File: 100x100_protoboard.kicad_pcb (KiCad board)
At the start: 2 copper layers, 97.8 x 96.5 mm, 418 parts, among them CON1 BARREL_JACK, CON2 USB_FEMALE_WITH_ID, CON3 USB_FEMALE_WITH_ID, J1 INTERCONNECT_1X03, J10 INTERCONNECT_1X03, J11 INTERCONNECT_1X03, J12 INTERCONNECT_1X03, J13 INTERCONNECT_1X03, J14 INTERCONNECT_1X03, J15 INTERCONNECT_1X03, J16 INTERCONNECT_1X03, J17 INTERCONNECT_1X03, J18 INTERCONNECT_1X03, J19 INTERCONNECT_1X03, J2 INTERCONNECT_1X03, J20 INTERCONNECT_1X03, J21 INTERCONNECT_1X03, J22 INTERCONNECT_1X03, J23 INTERCONNECT_1X03, J24 INTERCONNECT_1X03, J25 INTERCONNECT_1X03, J26 INTERCONNECT_1X03, J27 INTERCONNECT_1X03, J28 INTERCONNECT_1X03, J29 INTERCONNECT_1X03, J3 INTERCONNECT_1X03, J30 INTERCONNECT_1X03, J31 INTERCONNECT_1X03, J32 INTERCONNECT_1X03, J33 INTERCONNECT_1X03, J34 INTERCONNECT_1X03, J35 INTERCONNECT_1X03, J36 INTERCONNECT_1X03, J37 INTERCONNECT_1X03, J38 INTERCONNECT_1X03, J39 INTERCONNECT_1X03, J4 INTERCONNECT_1X03, J40 INTERCONNECT_1X03, J41 INTERCONNECT_1X03, J42 INTERCONNECT_1X03, J43 INTERCONNECT_1X03, J44 INTERCONNECT_1X03, J45 INTERCONNECT_1X03, J46 INTERCONNECT_1X03, J47 INTERCONNECT_1X03, J48 INTERCONNECT_1X03, J49 INTERCONNECT_1X03, J5 INTERCONNECT_1X03, J50 INTERCONNECT_1X03, J51 INTERCONNECT_1X03, J52 INTERCONNECT_1X03, J53 INTERCONNECT_1X03, J54 INTERCONNECT_1X03, J55 INTERCONNECT_1X03, J56 INTERCONNECT_1X03, J57 INTERCONNECT_1X03, J58 INTERCONNECT_1X03, J59 INTERCONNECT_1X03, J6 INTERCONNECT_1X03, J60 INTERCONNECT_1X03, J61 INTERCONNECT_1X03, J62 INTERCONNECT_1X03, J63 INTERCONNECT_1X03, J64 INTERCONNECT_1X03, J65 INTERCONNECT_1X02, J7 INTERCONNECT_1X03, J8 INTERCONNECT_1X03, J9 INTERCONNECT_1X03, P1 CONN_5, P1 CONN_8X2, P2 CONN_8X2, U1 LM7805CT

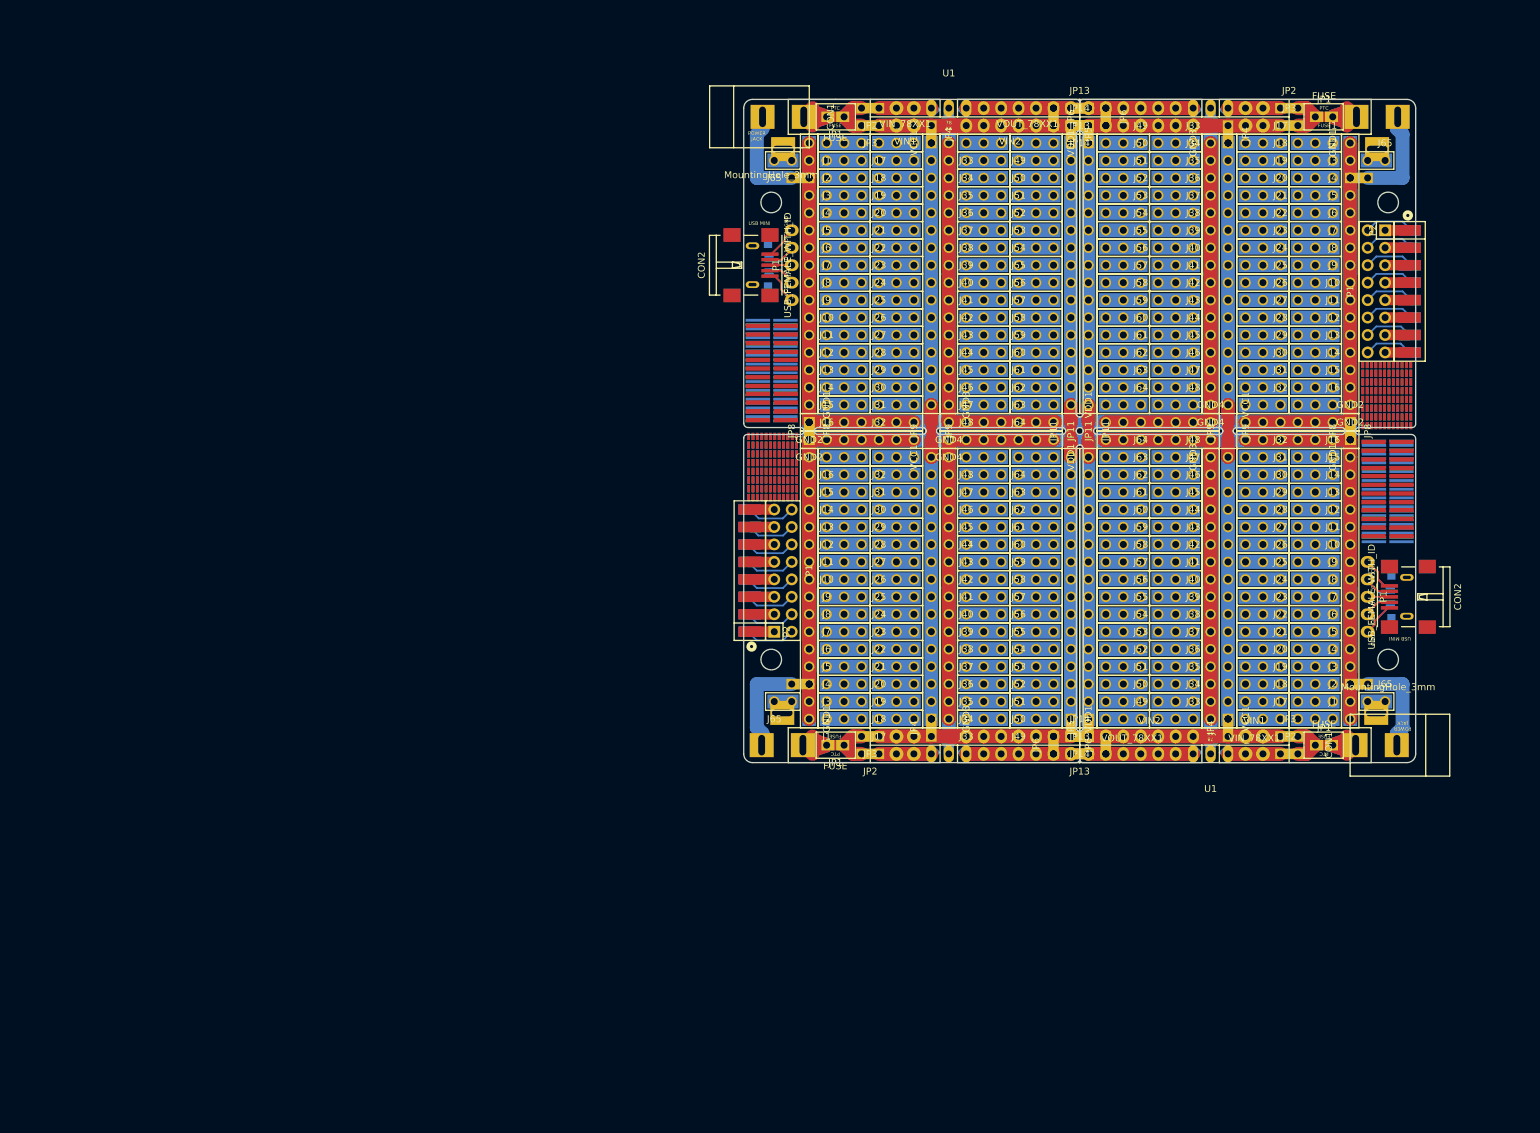
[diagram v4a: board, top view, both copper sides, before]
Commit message: flipped the outermost power rail solder jumper, so that all of these solder-jumpers are shorted on the front
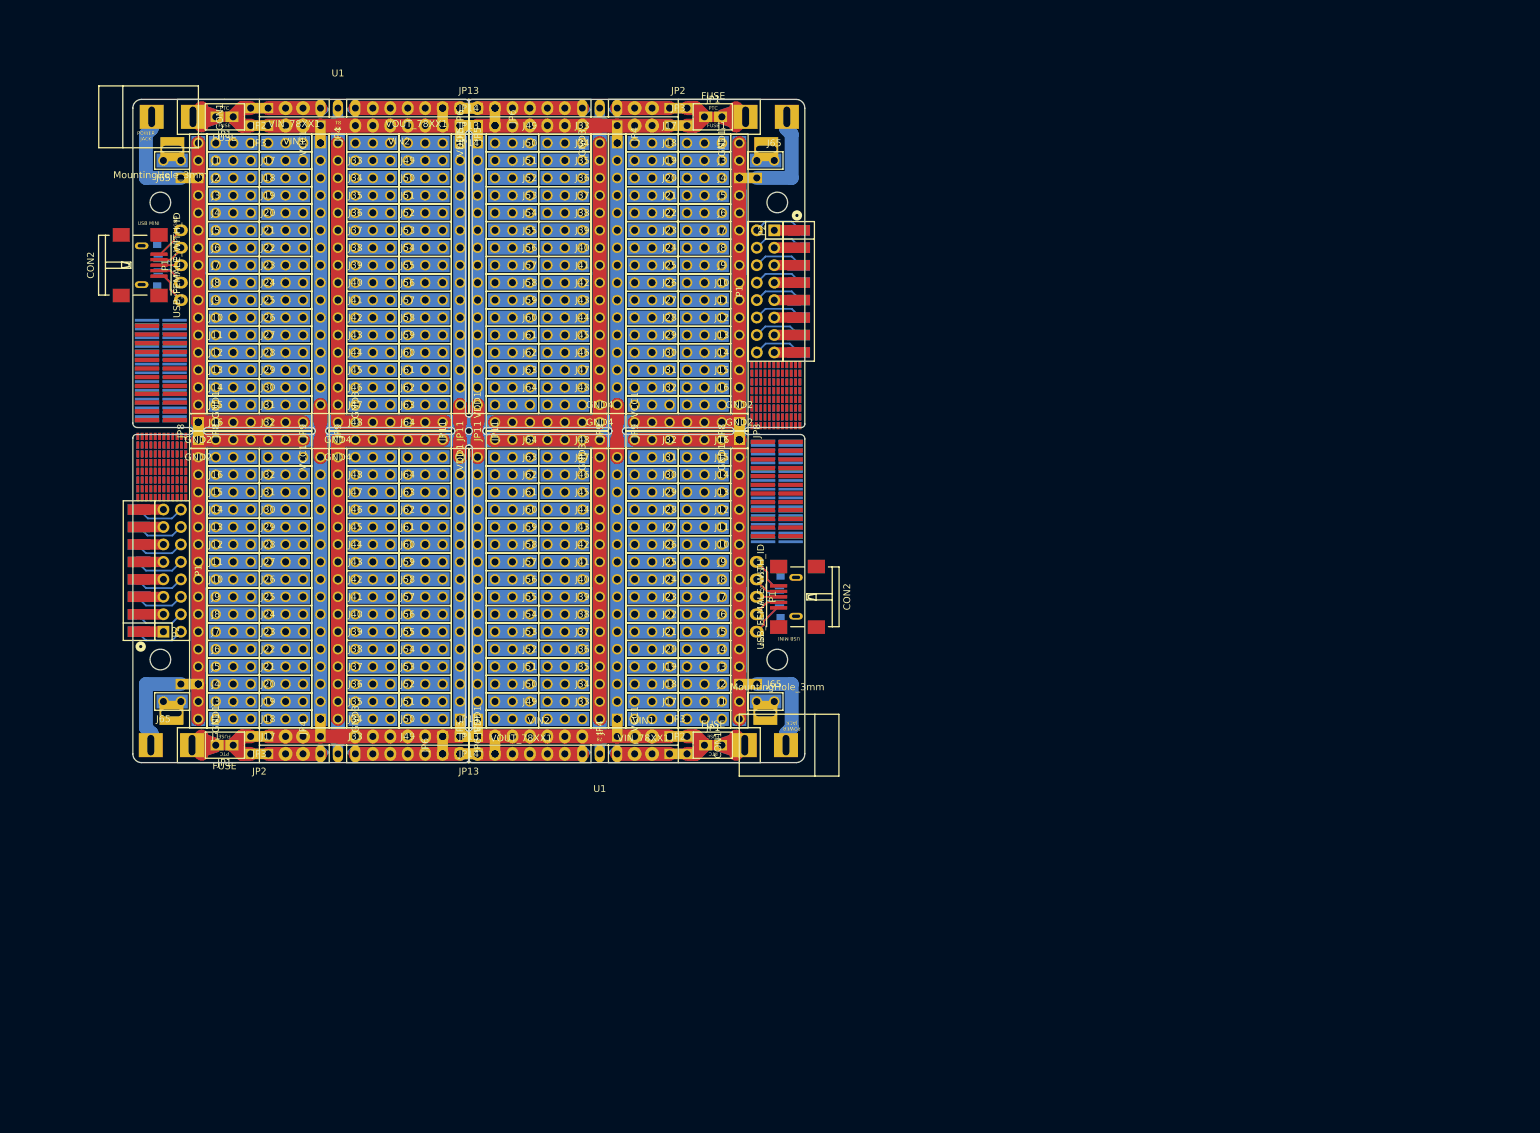
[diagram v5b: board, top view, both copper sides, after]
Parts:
- removed the C1 at (190.5, 32.8)
- removed the C1 at (190.5, 124.7)
- removed the C2 at (188.0, 32.8)
- removed the C2 at (188.0, 124.7)
- removed the CON1 at (216.7, 33.0)
- removed the CON1 at (216.5, 124.5)
- removed the F1 at (205.7, 33.0)
- removed the F1 at (205.7, 124.5)
- removed the F2 at (205.7, 33.0)
- removed the F2 at (205.7, 124.5)
- removed the GND1 at (209.6, 36.8)
- removed the GND1 at (209.6, 82.5)
- removed the GND2 at (209.6, 77.5)
- removed the GND2 at (209.6, 80.0)
- removed the GND3 at (189.2, 36.8)
- removed the GND3 at (189.2, 82.5)
- removed the GND4 at (189.2, 77.5)
- removed the GND4 at (189.2, 80.0)
- removed the J1 at (207.0, 36.8)
- removed the J1 at (207.0, 120.7)
- removed the J10 at (207.0, 59.7)
- removed the J10 at (207.0, 97.8)
- removed the J11 at (207.0, 62.2)
- removed the J11 at (207.0, 95.2)
- removed the J12 at (207.0, 64.8)
- removed the J12 at (207.0, 92.7)
- removed the J13 at (207.0, 67.3)
- removed the J13 at (207.0, 90.2)
- removed the J14 at (207.0, 69.8)
- removed the J14 at (207.0, 87.6)
- removed the J15 at (207.0, 72.4)
- removed the J15 at (207.0, 85.1)
- removed the J16 at (207.0, 74.9)
- removed the J16 at (207.0, 82.5)
- removed the J17 at (199.4, 36.8)
- removed the J17 at (199.4, 120.7)
- removed the J18 at (199.4, 39.4)
- removed the J18 at (199.4, 118.1)
- removed the J19 at (199.4, 41.9)
- removed the J19 at (199.4, 115.6)
- removed the J2 at (207.0, 39.4)
- removed the J2 at (207.0, 118.1)
- removed the J20 at (199.4, 44.5)
- removed the J20 at (199.4, 113.0)
- removed the J21 at (199.4, 47.0)
- removed the J21 at (199.4, 110.5)
- removed the J22 at (199.4, 49.5)
- removed the J22 at (199.4, 108.0)
- removed the J23 at (199.4, 52.1)
- removed the J23 at (199.4, 105.4)
- removed the J24 at (199.4, 54.6)
- removed the J24 at (199.4, 102.9)
- removed the J25 at (199.4, 57.1)
- removed the J25 at (199.4, 100.3)
- removed the J26 at (199.4, 59.7)
- removed the J26 at (199.4, 97.8)
- removed the J27 at (199.4, 62.2)
- removed the J27 at (199.4, 95.2)
- removed the J28 at (199.4, 64.8)
- removed the J28 at (199.4, 92.7)
- removed the J29 at (199.4, 67.3)
- removed the J29 at (199.4, 90.2)
- removed the J3 at (207.0, 41.9)
- removed the J3 at (207.0, 115.6)
- removed the J30 at (199.4, 69.8)
- removed the J30 at (199.4, 87.6)
- removed the J31 at (199.4, 72.4)
- removed the J31 at (199.4, 85.1)
- removed the J32 at (199.4, 74.9)
- removed the J32 at (199.4, 82.5)
- removed the J33 at (186.7, 36.8)
- removed the J33 at (186.7, 120.7)
- removed the J34 at (186.7, 39.4)
- removed the J34 at (186.7, 118.1)
- removed the J35 at (186.7, 41.9)
- removed the J35 at (186.7, 115.6)
- removed the J36 at (186.7, 44.5)
- removed the J36 at (186.7, 113.0)
- removed the J37 at (186.7, 47.0)
- removed the J37 at (186.7, 110.5)
- removed the J38 at (186.7, 49.5)
- removed the J38 at (186.7, 108.0)
- removed the J39 at (186.7, 52.1)
- removed the J39 at (186.7, 105.4)
- removed the J4 at (207.0, 44.5)
- removed the J4 at (207.0, 113.0)
- removed the J40 at (186.7, 54.6)
- removed the J40 at (186.7, 102.9)
- removed the J41 at (186.7, 57.1)
- removed the J41 at (186.7, 100.3)
- removed the J42 at (186.7, 59.7)
- removed the J42 at (186.7, 97.8)
- removed the J43 at (186.7, 62.2)
- removed the J43 at (186.7, 95.2)
- removed the J44 at (186.7, 64.8)
- removed the J44 at (186.7, 92.7)
- removed the J45 at (186.7, 67.3)
- removed the J45 at (186.7, 90.2)
- removed the J46 at (186.7, 69.8)
- removed the J46 at (186.7, 87.6)
- removed the J47 at (186.7, 72.4)
- removed the J47 at (186.7, 85.1)
- removed the J48 at (186.7, 74.9)
- removed the J48 at (186.7, 82.5)
- removed the J49 at (179.1, 36.8)
- removed the J49 at (179.1, 120.7)
- removed the J5 at (207.0, 47.0)
- removed the J5 at (207.0, 110.5)
- removed the J50 at (179.1, 39.4)
- removed the J50 at (179.1, 118.1)
- removed the J51 at (179.1, 41.9)
- removed the J51 at (179.1, 115.6)
- removed the J52 at (179.1, 44.5)
- removed the J52 at (179.1, 113.0)
- removed the J53 at (179.1, 47.0)
- removed the J53 at (179.1, 110.5)
- removed the J54 at (179.1, 49.5)
- removed the J54 at (179.1, 108.0)
- removed the J55 at (179.1, 52.1)
- removed the J55 at (179.1, 105.4)
- removed the J56 at (179.1, 54.6)
- removed the J56 at (179.1, 102.9)
- removed the J57 at (179.1, 57.1)
- removed the J57 at (179.1, 100.3)
- removed the J58 at (179.1, 59.7)
- removed the J58 at (179.1, 97.8)
- removed the J59 at (179.1, 62.2)
- removed the J59 at (179.1, 95.2)
- removed the J6 at (207.0, 49.5)
- removed the J6 at (207.0, 108.0)
- removed the J60 at (179.1, 64.8)
- removed the J60 at (179.1, 92.7)
- removed the J61 at (179.1, 67.3)
- removed the J61 at (179.1, 90.2)
- removed the J62 at (179.1, 69.8)
- removed the J62 at (179.1, 87.6)
- removed the J63 at (179.1, 72.4)
- removed the J63 at (179.1, 85.1)
- removed the J64 at (179.1, 74.9)
- removed the J64 at (179.1, 82.5)
- removed the J65 at (214.6, 39.4)
- removed the J65 at (214.6, 118.1)
- removed the J7 at (207.0, 52.1)
- removed the J7 at (207.0, 105.4)
- removed the J8 at (207.0, 54.6)
- removed the J8 at (207.0, 102.9)
- removed the J9 at (207.0, 57.1)
- removed the J9 at (207.0, 100.3)
- removed the JP1 at (205.7, 33.0)
- removed the JP1 at (205.7, 124.5)
- removed the JP10 at (171.4, 78.7) (x2)
- removed the JP11 at (171.4, 78.7) (x2)
- removed the JP12 at (170.2, 77.5)
- removed the JP12 at (170.2, 80.0)
- removed the JP13 at (170.2, 31.8)
- removed the JP13 at (170.2, 125.7)
- removed the JP14 at (170.2, 34.3)
- removed the JP14 at (170.2, 123.2)
- removed the JP15 at (191.8, 78.7) (x2)
- removed the JP2 at (200.7, 31.8)
- removed the JP2 at (200.7, 125.7)
- removed the JP3 at (200.7, 34.3)
- removed the JP3 at (200.7, 123.2)
- removed the JP4 at (191.8, 35.6)
- removed the JP4 at (191.8, 121.9)
- removed the JP5 at (171.4, 35.6)
- removed the JP5 at (171.4, 121.9)
- removed the JP6 at (174.0, 33.0)
- removed the JP6 at (174.0, 124.5)
- removed the JP7 at (210.8, 41.9)
- removed the JP7 at (210.8, 115.6)
- removed the JP8 at (209.6, 78.7) (x2)
- removed the JP9 at (191.8, 78.7) (x2)
- removed the MountingHole_3mm at (215.1, 45.5)
- removed the MountingHole_3mm at (215.1, 112.0)
- removed the P1 at (213.4, 58.4)
- removed the P1 at (212.1, 102.9)
- removed the Ref** at (215.5, 76.0) (x2)
- removed the Ref** at (215.0, 92.6)
- removed the Ref** at (215.5, 71.0) (x2)
- removed the Ref** at (215.0, 92.2)
- removed the Ref** at (215.0, 87.2)
- removed the Ref** at (215.0, 82.2)
- removed the Ref** at (215.0, 82.4)
- removed the Ref** at (215.0, 87.5)
- removed the U1 at (189.2, 31.8)
- removed the U1 at (189.2, 125.7)
- removed the VCC1 at (191.8, 74.9)
- removed the VCC1 at (191.8, 120.7)
- removed the VDD1 at (171.4, 36.8)
- removed the VDD1 at (171.4, 82.5)
- removed the VIN1 at (195.6, 34.3)
- removed the VIN1 at (195.6, 123.2)
- removed the VIN2 at (180.3, 34.3)
- removed the VIN2 at (180.3, 123.2)
- removed the VIN_78XX1 at (195.6, 31.8)
- removed the VIN_78XX1 at (195.6, 125.7)
- removed the VOUT_78XX1 at (177.8, 31.8)
- removed the VOUT_78XX1 at (177.8, 125.7)
- added C1: u33, Capacitors_SMD:C_0805_HandSoldering, B.Cu at (101.6, 32.8)
- added C1: u33, Capacitors_SMD:C_0805_HandSoldering, B.Cu at (101.6, 124.7)
- added C2: u1, Capacitors_SMD:C_0805_HandSoldering, B.Cu at (99.1, 32.8)
- added C2: u1, Capacitors_SMD:C_0805_HandSoldering, B.Cu at (99.1, 124.7)
- added CON1: BARREL_JACK, Connect:BARREL_JACK, B.Cu at (127.8, 33.0)
- added CON1: BARREL_JACK, Connect:BARREL_JACK, F.Cu at (127.6, 124.5)
- added F1: FUSE, Muonde:CC12ZZ, B.Cu at (116.8, 33.0)
- added F1: FUSE, Muonde:CC12ZZ, F.Cu at (116.8, 124.5)
- added F2: FUSE, Muonde:CC12ZZ, F.Cu at (116.8, 33.0)
- added F2: FUSE, Muonde:CC12ZZ, B.Cu at (116.8, 124.5)
- added GND1: INTERCONNECT_1X16, 2.54mm_Pin_Headers:Interconnect_1x16, F.Cu at (120.7, 36.8)
- added GND1: INTERCONNECT_1X16, 2.54mm_Pin_Headers:Interconnect_1x16, F.Cu at (120.7, 82.5)
- added GND2: INTERCONNECT_1X07, 2.54mm_Pin_Headers:Interconnect_1x07, F.Cu at (120.7, 77.5)
- added GND2: INTERCONNECT_1X07, 2.54mm_Pin_Headers:Interconnect_1x07, F.Cu at (120.7, 80.0)
- added GND3: INTERCONNECT_1X16, 2.54mm_Pin_Headers:Interconnect_1x16, F.Cu at (100.3, 36.8)
- added GND3: INTERCONNECT_1X16, 2.54mm_Pin_Headers:Interconnect_1x16, F.Cu at (100.3, 82.5)
- added GND4: INTERCONNECT_1X07, 2.54mm_Pin_Headers:Interconnect_1x07, F.Cu at (100.3, 77.5)
- added GND4: INTERCONNECT_1X07, 2.54mm_Pin_Headers:Interconnect_1x07, F.Cu at (100.3, 80.0)
- added J1: INTERCONNECT_1X03, 2.54mm_Pin_Headers:Interconnect_1x03, F.Cu at (118.1, 36.8)
- added J1: INTERCONNECT_1X03, 2.54mm_Pin_Headers:Interconnect_1x03, F.Cu at (118.1, 120.7)
- added J10: INTERCONNECT_1X03, 2.54mm_Pin_Headers:Interconnect_1x03, F.Cu at (118.1, 59.7)
- added J10: INTERCONNECT_1X03, 2.54mm_Pin_Headers:Interconnect_1x03, F.Cu at (118.1, 97.8)
- added J11: INTERCONNECT_1X03, 2.54mm_Pin_Headers:Interconnect_1x03, F.Cu at (118.1, 62.2)
- added J11: INTERCONNECT_1X03, 2.54mm_Pin_Headers:Interconnect_1x03, F.Cu at (118.1, 95.2)
- added J12: INTERCONNECT_1X03, 2.54mm_Pin_Headers:Interconnect_1x03, F.Cu at (118.1, 64.8)
- added J12: INTERCONNECT_1X03, 2.54mm_Pin_Headers:Interconnect_1x03, F.Cu at (118.1, 92.7)
- added J13: INTERCONNECT_1X03, 2.54mm_Pin_Headers:Interconnect_1x03, F.Cu at (118.1, 67.3)
- added J13: INTERCONNECT_1X03, 2.54mm_Pin_Headers:Interconnect_1x03, F.Cu at (118.1, 90.2)
- added J14: INTERCONNECT_1X03, 2.54mm_Pin_Headers:Interconnect_1x03, F.Cu at (118.1, 69.8)
- added J14: INTERCONNECT_1X03, 2.54mm_Pin_Headers:Interconnect_1x03, F.Cu at (118.1, 87.6)
- added J15: INTERCONNECT_1X03, 2.54mm_Pin_Headers:Interconnect_1x03, F.Cu at (118.1, 72.4)
- added J15: INTERCONNECT_1X03, 2.54mm_Pin_Headers:Interconnect_1x03, F.Cu at (118.1, 85.1)
- added J16: INTERCONNECT_1X03, 2.54mm_Pin_Headers:Interconnect_1x03, F.Cu at (118.1, 74.9)
- added J16: INTERCONNECT_1X03, 2.54mm_Pin_Headers:Interconnect_1x03, F.Cu at (118.1, 82.5)
- added J17: INTERCONNECT_1X03, 2.54mm_Pin_Headers:Interconnect_1x03, F.Cu at (110.5, 36.8)
- added J17: INTERCONNECT_1X03, 2.54mm_Pin_Headers:Interconnect_1x03, F.Cu at (110.5, 120.7)
- added J18: INTERCONNECT_1X03, 2.54mm_Pin_Headers:Interconnect_1x03, F.Cu at (110.5, 39.4)
- added J18: INTERCONNECT_1X03, 2.54mm_Pin_Headers:Interconnect_1x03, F.Cu at (110.5, 118.1)
- added J19: INTERCONNECT_1X03, 2.54mm_Pin_Headers:Interconnect_1x03, F.Cu at (110.5, 41.9)
- added J19: INTERCONNECT_1X03, 2.54mm_Pin_Headers:Interconnect_1x03, F.Cu at (110.5, 115.6)
- added J2: INTERCONNECT_1X03, 2.54mm_Pin_Headers:Interconnect_1x03, F.Cu at (118.1, 39.4)
- added J2: INTERCONNECT_1X03, 2.54mm_Pin_Headers:Interconnect_1x03, F.Cu at (118.1, 118.1)
- added J20: INTERCONNECT_1X03, 2.54mm_Pin_Headers:Interconnect_1x03, F.Cu at (110.5, 44.5)
- added J20: INTERCONNECT_1X03, 2.54mm_Pin_Headers:Interconnect_1x03, F.Cu at (110.5, 113.0)
- added J21: INTERCONNECT_1X03, 2.54mm_Pin_Headers:Interconnect_1x03, F.Cu at (110.5, 47.0)
- added J21: INTERCONNECT_1X03, 2.54mm_Pin_Headers:Interconnect_1x03, F.Cu at (110.5, 110.5)
- added J22: INTERCONNECT_1X03, 2.54mm_Pin_Headers:Interconnect_1x03, F.Cu at (110.5, 49.5)
- added J22: INTERCONNECT_1X03, 2.54mm_Pin_Headers:Interconnect_1x03, F.Cu at (110.5, 108.0)
- added J23: INTERCONNECT_1X03, 2.54mm_Pin_Headers:Interconnect_1x03, F.Cu at (110.5, 52.1)
- added J23: INTERCONNECT_1X03, 2.54mm_Pin_Headers:Interconnect_1x03, F.Cu at (110.5, 105.4)
- added J24: INTERCONNECT_1X03, 2.54mm_Pin_Headers:Interconnect_1x03, F.Cu at (110.5, 54.6)
- added J24: INTERCONNECT_1X03, 2.54mm_Pin_Headers:Interconnect_1x03, F.Cu at (110.5, 102.9)
- added J25: INTERCONNECT_1X03, 2.54mm_Pin_Headers:Interconnect_1x03, F.Cu at (110.5, 57.1)
- added J25: INTERCONNECT_1X03, 2.54mm_Pin_Headers:Interconnect_1x03, F.Cu at (110.5, 100.3)
- added J26: INTERCONNECT_1X03, 2.54mm_Pin_Headers:Interconnect_1x03, F.Cu at (110.5, 59.7)
- added J26: INTERCONNECT_1X03, 2.54mm_Pin_Headers:Interconnect_1x03, F.Cu at (110.5, 97.8)
- added J27: INTERCONNECT_1X03, 2.54mm_Pin_Headers:Interconnect_1x03, F.Cu at (110.5, 62.2)
- added J27: INTERCONNECT_1X03, 2.54mm_Pin_Headers:Interconnect_1x03, F.Cu at (110.5, 95.2)
- added J28: INTERCONNECT_1X03, 2.54mm_Pin_Headers:Interconnect_1x03, F.Cu at (110.5, 64.8)
- added J28: INTERCONNECT_1X03, 2.54mm_Pin_Headers:Interconnect_1x03, F.Cu at (110.5, 92.7)
- added J29: INTERCONNECT_1X03, 2.54mm_Pin_Headers:Interconnect_1x03, F.Cu at (110.5, 67.3)
- added J29: INTERCONNECT_1X03, 2.54mm_Pin_Headers:Interconnect_1x03, F.Cu at (110.5, 90.2)
- added J3: INTERCONNECT_1X03, 2.54mm_Pin_Headers:Interconnect_1x03, F.Cu at (118.1, 41.9)
- added J3: INTERCONNECT_1X03, 2.54mm_Pin_Headers:Interconnect_1x03, F.Cu at (118.1, 115.6)
- added J30: INTERCONNECT_1X03, 2.54mm_Pin_Headers:Interconnect_1x03, F.Cu at (110.5, 69.8)
- added J30: INTERCONNECT_1X03, 2.54mm_Pin_Headers:Interconnect_1x03, F.Cu at (110.5, 87.6)
- added J31: INTERCONNECT_1X03, 2.54mm_Pin_Headers:Interconnect_1x03, F.Cu at (110.5, 72.4)
- added J31: INTERCONNECT_1X03, 2.54mm_Pin_Headers:Interconnect_1x03, F.Cu at (110.5, 85.1)
- added J32: INTERCONNECT_1X03, 2.54mm_Pin_Headers:Interconnect_1x03, F.Cu at (110.5, 74.9)
- added J32: INTERCONNECT_1X03, 2.54mm_Pin_Headers:Interconnect_1x03, F.Cu at (110.5, 82.5)
- added J33: INTERCONNECT_1X03, 2.54mm_Pin_Headers:Interconnect_1x03, F.Cu at (97.8, 36.8)
- added J33: INTERCONNECT_1X03, 2.54mm_Pin_Headers:Interconnect_1x03, F.Cu at (97.8, 120.7)
- added J34: INTERCONNECT_1X03, 2.54mm_Pin_Headers:Interconnect_1x03, F.Cu at (97.8, 39.4)
- added J34: INTERCONNECT_1X03, 2.54mm_Pin_Headers:Interconnect_1x03, F.Cu at (97.8, 118.1)
- added J35: INTERCONNECT_1X03, 2.54mm_Pin_Headers:Interconnect_1x03, F.Cu at (97.8, 41.9)
- added J35: INTERCONNECT_1X03, 2.54mm_Pin_Headers:Interconnect_1x03, F.Cu at (97.8, 115.6)
- added J36: INTERCONNECT_1X03, 2.54mm_Pin_Headers:Interconnect_1x03, F.Cu at (97.8, 44.5)
- added J36: INTERCONNECT_1X03, 2.54mm_Pin_Headers:Interconnect_1x03, F.Cu at (97.8, 113.0)
- added J37: INTERCONNECT_1X03, 2.54mm_Pin_Headers:Interconnect_1x03, F.Cu at (97.8, 47.0)
- added J37: INTERCONNECT_1X03, 2.54mm_Pin_Headers:Interconnect_1x03, F.Cu at (97.8, 110.5)
- added J38: INTERCONNECT_1X03, 2.54mm_Pin_Headers:Interconnect_1x03, F.Cu at (97.8, 49.5)
- added J38: INTERCONNECT_1X03, 2.54mm_Pin_Headers:Interconnect_1x03, F.Cu at (97.8, 108.0)
- added J39: INTERCONNECT_1X03, 2.54mm_Pin_Headers:Interconnect_1x03, F.Cu at (97.8, 52.1)
- added J39: INTERCONNECT_1X03, 2.54mm_Pin_Headers:Interconnect_1x03, F.Cu at (97.8, 105.4)
- added J4: INTERCONNECT_1X03, 2.54mm_Pin_Headers:Interconnect_1x03, F.Cu at (118.1, 44.5)
- added J4: INTERCONNECT_1X03, 2.54mm_Pin_Headers:Interconnect_1x03, F.Cu at (118.1, 113.0)
- added J40: INTERCONNECT_1X03, 2.54mm_Pin_Headers:Interconnect_1x03, F.Cu at (97.8, 54.6)
- added J40: INTERCONNECT_1X03, 2.54mm_Pin_Headers:Interconnect_1x03, F.Cu at (97.8, 102.9)
- added J41: INTERCONNECT_1X03, 2.54mm_Pin_Headers:Interconnect_1x03, F.Cu at (97.8, 57.1)
- added J41: INTERCONNECT_1X03, 2.54mm_Pin_Headers:Interconnect_1x03, F.Cu at (97.8, 100.3)
- added J42: INTERCONNECT_1X03, 2.54mm_Pin_Headers:Interconnect_1x03, F.Cu at (97.8, 59.7)
- added J42: INTERCONNECT_1X03, 2.54mm_Pin_Headers:Interconnect_1x03, F.Cu at (97.8, 97.8)
- added J43: INTERCONNECT_1X03, 2.54mm_Pin_Headers:Interconnect_1x03, F.Cu at (97.8, 62.2)
- added J43: INTERCONNECT_1X03, 2.54mm_Pin_Headers:Interconnect_1x03, F.Cu at (97.8, 95.2)
- added J44: INTERCONNECT_1X03, 2.54mm_Pin_Headers:Interconnect_1x03, F.Cu at (97.8, 64.8)
- added J44: INTERCONNECT_1X03, 2.54mm_Pin_Headers:Interconnect_1x03, F.Cu at (97.8, 92.7)
- added J45: INTERCONNECT_1X03, 2.54mm_Pin_Headers:Interconnect_1x03, F.Cu at (97.8, 67.3)
- added J45: INTERCONNECT_1X03, 2.54mm_Pin_Headers:Interconnect_1x03, F.Cu at (97.8, 90.2)
- added J46: INTERCONNECT_1X03, 2.54mm_Pin_Headers:Interconnect_1x03, F.Cu at (97.8, 69.8)
- added J46: INTERCONNECT_1X03, 2.54mm_Pin_Headers:Interconnect_1x03, F.Cu at (97.8, 87.6)
- added J47: INTERCONNECT_1X03, 2.54mm_Pin_Headers:Interconnect_1x03, F.Cu at (97.8, 72.4)
- added J47: INTERCONNECT_1X03, 2.54mm_Pin_Headers:Interconnect_1x03, F.Cu at (97.8, 85.1)
- added J48: INTERCONNECT_1X03, 2.54mm_Pin_Headers:Interconnect_1x03, F.Cu at (97.8, 74.9)
- added J48: INTERCONNECT_1X03, 2.54mm_Pin_Headers:Interconnect_1x03, F.Cu at (97.8, 82.5)
- added J49: INTERCONNECT_1X03, 2.54mm_Pin_Headers:Interconnect_1x03, F.Cu at (90.2, 36.8)
- added J49: INTERCONNECT_1X03, 2.54mm_Pin_Headers:Interconnect_1x03, F.Cu at (90.2, 120.7)
- added J5: INTERCONNECT_1X03, 2.54mm_Pin_Headers:Interconnect_1x03, F.Cu at (118.1, 47.0)
- added J5: INTERCONNECT_1X03, 2.54mm_Pin_Headers:Interconnect_1x03, F.Cu at (118.1, 110.5)
- added J50: INTERCONNECT_1X03, 2.54mm_Pin_Headers:Interconnect_1x03, F.Cu at (90.2, 39.4)
- added J50: INTERCONNECT_1X03, 2.54mm_Pin_Headers:Interconnect_1x03, F.Cu at (90.2, 118.1)
- added J51: INTERCONNECT_1X03, 2.54mm_Pin_Headers:Interconnect_1x03, F.Cu at (90.2, 41.9)
- added J51: INTERCONNECT_1X03, 2.54mm_Pin_Headers:Interconnect_1x03, F.Cu at (90.2, 115.6)
- added J52: INTERCONNECT_1X03, 2.54mm_Pin_Headers:Interconnect_1x03, F.Cu at (90.2, 44.5)
- added J52: INTERCONNECT_1X03, 2.54mm_Pin_Headers:Interconnect_1x03, F.Cu at (90.2, 113.0)
- added J53: INTERCONNECT_1X03, 2.54mm_Pin_Headers:Interconnect_1x03, F.Cu at (90.2, 47.0)
- added J53: INTERCONNECT_1X03, 2.54mm_Pin_Headers:Interconnect_1x03, F.Cu at (90.2, 110.5)
- added J54: INTERCONNECT_1X03, 2.54mm_Pin_Headers:Interconnect_1x03, F.Cu at (90.2, 49.5)
- added J54: INTERCONNECT_1X03, 2.54mm_Pin_Headers:Interconnect_1x03, F.Cu at (90.2, 108.0)
- added J55: INTERCONNECT_1X03, 2.54mm_Pin_Headers:Interconnect_1x03, F.Cu at (90.2, 52.1)
- added J55: INTERCONNECT_1X03, 2.54mm_Pin_Headers:Interconnect_1x03, F.Cu at (90.2, 105.4)
- added J56: INTERCONNECT_1X03, 2.54mm_Pin_Headers:Interconnect_1x03, F.Cu at (90.2, 54.6)
- added J56: INTERCONNECT_1X03, 2.54mm_Pin_Headers:Interconnect_1x03, F.Cu at (90.2, 102.9)
- added J57: INTERCONNECT_1X03, 2.54mm_Pin_Headers:Interconnect_1x03, F.Cu at (90.2, 57.1)
- added J57: INTERCONNECT_1X03, 2.54mm_Pin_Headers:Interconnect_1x03, F.Cu at (90.2, 100.3)
- added J58: INTERCONNECT_1X03, 2.54mm_Pin_Headers:Interconnect_1x03, F.Cu at (90.2, 59.7)
- added J58: INTERCONNECT_1X03, 2.54mm_Pin_Headers:Interconnect_1x03, F.Cu at (90.2, 97.8)
- added J59: INTERCONNECT_1X03, 2.54mm_Pin_Headers:Interconnect_1x03, F.Cu at (90.2, 62.2)
- added J59: INTERCONNECT_1X03, 2.54mm_Pin_Headers:Interconnect_1x03, F.Cu at (90.2, 95.2)
- added J6: INTERCONNECT_1X03, 2.54mm_Pin_Headers:Interconnect_1x03, F.Cu at (118.1, 49.5)
- added J6: INTERCONNECT_1X03, 2.54mm_Pin_Headers:Interconnect_1x03, F.Cu at (118.1, 108.0)
- added J60: INTERCONNECT_1X03, 2.54mm_Pin_Headers:Interconnect_1x03, F.Cu at (90.2, 64.8)
- added J60: INTERCONNECT_1X03, 2.54mm_Pin_Headers:Interconnect_1x03, F.Cu at (90.2, 92.7)
- added J61: INTERCONNECT_1X03, 2.54mm_Pin_Headers:Interconnect_1x03, F.Cu at (90.2, 67.3)
- added J61: INTERCONNECT_1X03, 2.54mm_Pin_Headers:Interconnect_1x03, F.Cu at (90.2, 90.2)
- added J62: INTERCONNECT_1X03, 2.54mm_Pin_Headers:Interconnect_1x03, F.Cu at (90.2, 69.8)
- added J62: INTERCONNECT_1X03, 2.54mm_Pin_Headers:Interconnect_1x03, F.Cu at (90.2, 87.6)
- added J63: INTERCONNECT_1X03, 2.54mm_Pin_Headers:Interconnect_1x03, F.Cu at (90.2, 72.4)
- added J63: INTERCONNECT_1X03, 2.54mm_Pin_Headers:Interconnect_1x03, F.Cu at (90.2, 85.1)
- added J64: INTERCONNECT_1X03, 2.54mm_Pin_Headers:Interconnect_1x03, F.Cu at (90.2, 74.9)
- added J64: INTERCONNECT_1X03, 2.54mm_Pin_Headers:Interconnect_1x03, F.Cu at (90.2, 82.5)
- added J65: INTERCONNECT_1X02, 2.54mm_Pin_Headers:Interconnect_1x02, F.Cu at (125.7, 39.4)
- added J65: INTERCONNECT_1X02, 2.54mm_Pin_Headers:Interconnect_1x02, F.Cu at (125.7, 118.1)
- added J7: INTERCONNECT_1X03, 2.54mm_Pin_Headers:Interconnect_1x03, F.Cu at (118.1, 52.1)
- added J7: INTERCONNECT_1X03, 2.54mm_Pin_Headers:Interconnect_1x03, F.Cu at (118.1, 105.4)
- added J8: INTERCONNECT_1X03, 2.54mm_Pin_Headers:Interconnect_1x03, F.Cu at (118.1, 54.6)
- added J8: INTERCONNECT_1X03, 2.54mm_Pin_Headers:Interconnect_1x03, F.Cu at (118.1, 102.9)
- added J9: INTERCONNECT_1X03, 2.54mm_Pin_Headers:Interconnect_1x03, F.Cu at (118.1, 57.1)
- added J9: INTERCONNECT_1X03, 2.54mm_Pin_Headers:Interconnect_1x03, F.Cu at (118.1, 100.3)
- added JP1: JUMPER, 2.54mm_Pin_Headers:Solder_Jumper_1x2_Shorted_T, F.Cu at (116.8, 33.0)
- added JP1: JUMPER, 2.54mm_Pin_Headers:Solder_Jumper_1x2_Shorted_T, F.Cu at (116.8, 124.5)
- added JP10 (x2): JUMPER, 2.54mm_Pin_Headers:Solder_Jumper_SMD_1x2_Shorted, B.Cu at (82.5, 78.7)
- added JP11 (x2): JUMPER, 2.54mm_Pin_Headers:Solder_Jumper_SMD_1x2_Shorted, F.Cu at (82.5, 78.7)
- added JP12: JUMPER, 2.54mm_Pin_Headers:Solder_Jumper_SMD_1x2_Shorted, B.Cu at (81.3, 77.5)
- added JP12: JUMPER, 2.54mm_Pin_Headers:Solder_Jumper_SMD_1x2_Shorted, B.Cu at (81.3, 80.0)
- added JP13: JUMPER, 2.54mm_Pin_Headers:Solder_Jumper_1x2_Shorted_T, F.Cu at (81.3, 31.8)
- added JP13: JUMPER, 2.54mm_Pin_Headers:Solder_Jumper_1x2_Shorted_T, F.Cu at (81.3, 125.7)
- added JP14: JUMPER, 2.54mm_Pin_Headers:Solder_Jumper_1x2_Shorted_T, F.Cu at (81.3, 34.3)
- added JP14: JUMPER, 2.54mm_Pin_Headers:Solder_Jumper_1x2_Shorted_T, F.Cu at (81.3, 123.2)
- added JP15 (x2): JUMPER, 2.54mm_Pin_Headers:Solder_Jumper_SMD_1x2, B.Cu at (102.9, 78.7)
- added JP2: JUMPER, 2.54mm_Pin_Headers:Solder_Jumper_1x2_Shorted_T, F.Cu at (111.8, 31.8)
- added JP2: JUMPER, 2.54mm_Pin_Headers:Solder_Jumper_1x2_Shorted_T, F.Cu at (111.8, 125.7)
- added JP3: JUMPER, 2.54mm_Pin_Headers:Solder_Jumper_1x2_Shorted_T, F.Cu at (111.8, 34.3)
- added JP3: JUMPER, 2.54mm_Pin_Headers:Solder_Jumper_1x2_Shorted_T, F.Cu at (111.8, 123.2)
- added JP4: JUMPER, 2.54mm_Pin_Headers:Solder_Jumper_1x2_Shorted_T, F.Cu at (102.9, 35.6)
- added JP4: JUMPER, 2.54mm_Pin_Headers:Solder_Jumper_1x2_Shorted_T, F.Cu at (102.9, 121.9)
- added JP5: JUMPER, 2.54mm_Pin_Headers:Solder_Jumper_1x2_Shorted_T, F.Cu at (82.5, 35.6)
- added JP5: JUMPER, 2.54mm_Pin_Headers:Solder_Jumper_1x2_Shorted_T, F.Cu at (82.5, 121.9)
- added JP6: JUMPER, 2.54mm_Pin_Headers:Solder_Jumper_1x2_Shorted_T, F.Cu at (85.1, 33.0)
- added JP6: JUMPER, 2.54mm_Pin_Headers:Solder_Jumper_1x2_Shorted_T, F.Cu at (85.1, 124.5)
- added JP7: JUMPER, 2.54mm_Pin_Headers:Solder_Jumper_1x2_Shorted_T, B.Cu at (121.9, 41.9)
- added JP7: JUMPER, 2.54mm_Pin_Headers:Solder_Jumper_1x2_Shorted_T, B.Cu at (121.9, 115.6)
- added JP8 (x2): JUMPER, 2.54mm_Pin_Headers:Solder_Jumper_1x2, F.Cu at (120.7, 78.7)
- added JP9 (x2): JUMPER, 2.54mm_Pin_Headers:Solder_Jumper_SMD_1x2_Shorted, F.Cu at (102.9, 78.7)
- added MountingHole_3mm: VAL**, Mounting_Holes:MountingHole_3mm, B.Cu at (126.2, 45.5)
- added MountingHole_3mm: VAL**, Mounting_Holes:MountingHole_3mm, F.Cu at (126.2, 112.0)
- added P1: CONN_8X2, Socket_Strips:Socket_Strip_Straight_2x08, F.Cu at (124.5, 58.4)
- added P1: CONN_5, Socket_Strips:Socket_Strip_Straight_1x05, F.Cu at (123.2, 102.9)
- added Ref**: Val**, SMD:SMD_127_065_grid_4X12, F.Cu at (126.6, 76.0)
- added Ref**: Val**, SMD:SMD_065_357_8X2, B.Cu at (126.1, 92.6)
- added Ref**: Val**, SMD:SMD_127_065_grid_4X12, F.Cu at (126.6, 71.0)
- added Ref**: Val**, SMD:SMD_127_065_grid_4X12, B.Cu at (126.6, 76.0)
- added Ref**: Val**, SMD:SMD_127_065_grid_4X12, B.Cu at (126.6, 71.0)
- added Ref**: Val**, SMD:SMD_127_357_4X2, F.Cu at (126.1, 92.2)
- added Ref**: Val**, SMD:SMD_127_357_4X2, F.Cu at (126.1, 87.2)
- added Ref**: Val**, SMD:SMD_127_357_4X2, F.Cu at (126.1, 82.2)
- added Ref**: Val**, SMD:SMD_065_357_8X2, B.Cu at (126.1, 82.4)
- added Ref**: Val**, SMD:SMD_065_357_8X2, B.Cu at (126.1, 87.5)
- added U1: LM7805CT, Transistors_TO-220:TO-220_Neutral123_Vertical, B.Cu at (100.3, 31.8)
- added U1: LM7805CT, Transistors_TO-220:TO-220_Neutral123_Vertical, F.Cu at (100.3, 125.7)
- added VCC1: INTERCONNECT_1X16, 2.54mm_Pin_Headers:Interconnect_1x16, F.Cu at (102.9, 74.9)
- added VCC1: INTERCONNECT_1X16, 2.54mm_Pin_Headers:Interconnect_1x16, F.Cu at (102.9, 120.7)
- added VDD1: INTERCONNECT_1X16, 2.54mm_Pin_Headers:Interconnect_1x16, F.Cu at (82.5, 36.8)
- added VDD1: INTERCONNECT_1X16, 2.54mm_Pin_Headers:Interconnect_1x16, F.Cu at (82.5, 82.5)
- added VIN1: CONN_2, Socket_Strips:Socket_Strip_Straight_1x02, B.Cu at (106.7, 34.3)
- added VIN1: CONN_2, Socket_Strips:Socket_Strip_Straight_1x02, F.Cu at (106.7, 123.2)
- added VIN2: CONN_6, Socket_Strips:Socket_Strip_Straight_1x06, B.Cu at (91.4, 34.3)
- added VIN2: CONN_6, Socket_Strips:Socket_Strip_Straight_1x06, F.Cu at (91.4, 123.2)
- added VIN_78XX1: CONN_2, Socket_Strips:Socket_Strip_Straight_1x02, B.Cu at (106.7, 31.8)
- added VIN_78XX1: CONN_2, Socket_Strips:Socket_Strip_Straight_1x02, F.Cu at (106.7, 125.7)
- added VOUT_78XX1: CONN_6, Socket_Strips:Socket_Strip_Straight_1x06, B.Cu at (88.9, 31.8)
- added VOUT_78XX1: CONN_6, Socket_Strips:Socket_Strip_Straight_1x06, F.Cu at (88.9, 125.7)
- JP5: moved to F.Cu
- moved C1 88.9 mm to (61.0, 32.8)
- moved C1 88.9 mm to (61.0, 124.7)
- moved C2 88.9 mm to (63.5, 32.8)
- moved C2 88.9 mm to (63.5, 124.7)
- moved CON1 88.9 mm to (34.9, 33.0)
- moved CON2 88.9 mm to (36.2, 54.6)
- moved CON3 88.9 mm to (36.1, 54.6)
- moved F1 88.9 mm to (45.7, 33.0)
- moved F1 88.9 mm to (45.7, 124.5)
- moved F2 88.9 mm to (45.7, 33.0)
- moved F2 88.9 mm to (45.7, 124.5)
- moved GND1 88.9 mm to (41.9, 74.9)
- moved GND1 88.9 mm to (41.9, 120.7)
- moved GND2 88.9 mm to (41.9, 77.5)
- moved GND2 88.9 mm to (41.9, 80.0)
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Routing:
- net Net-(JP11-Pad1): track 7.62 -> 12.7 mm
- net Net-(JP14-Pad2): track 2.54 -> 0.00 mm
- net Net-(JP11-Pad2): track 2.54 -> 0.00 mm
